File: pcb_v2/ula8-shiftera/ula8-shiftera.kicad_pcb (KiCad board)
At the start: 2 copper layers, 54.4 x 61 mm, 17 parts, among them J1 ula8a, U1 74LS244, U2 74LS244, U3 74LS157, U4 74LS157

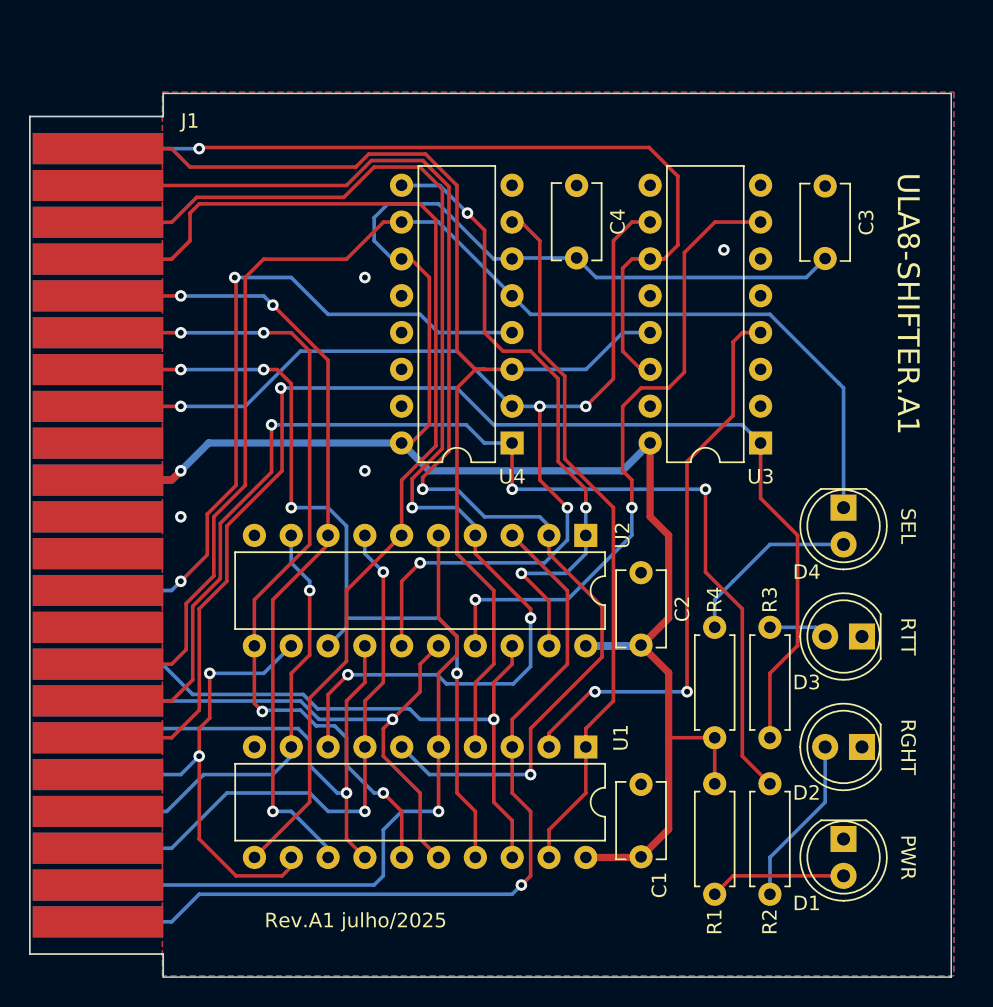
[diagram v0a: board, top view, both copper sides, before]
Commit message: revisao completa; mgrfa agora inclui sr8 e sgrda; remover estes dois no proximo commit
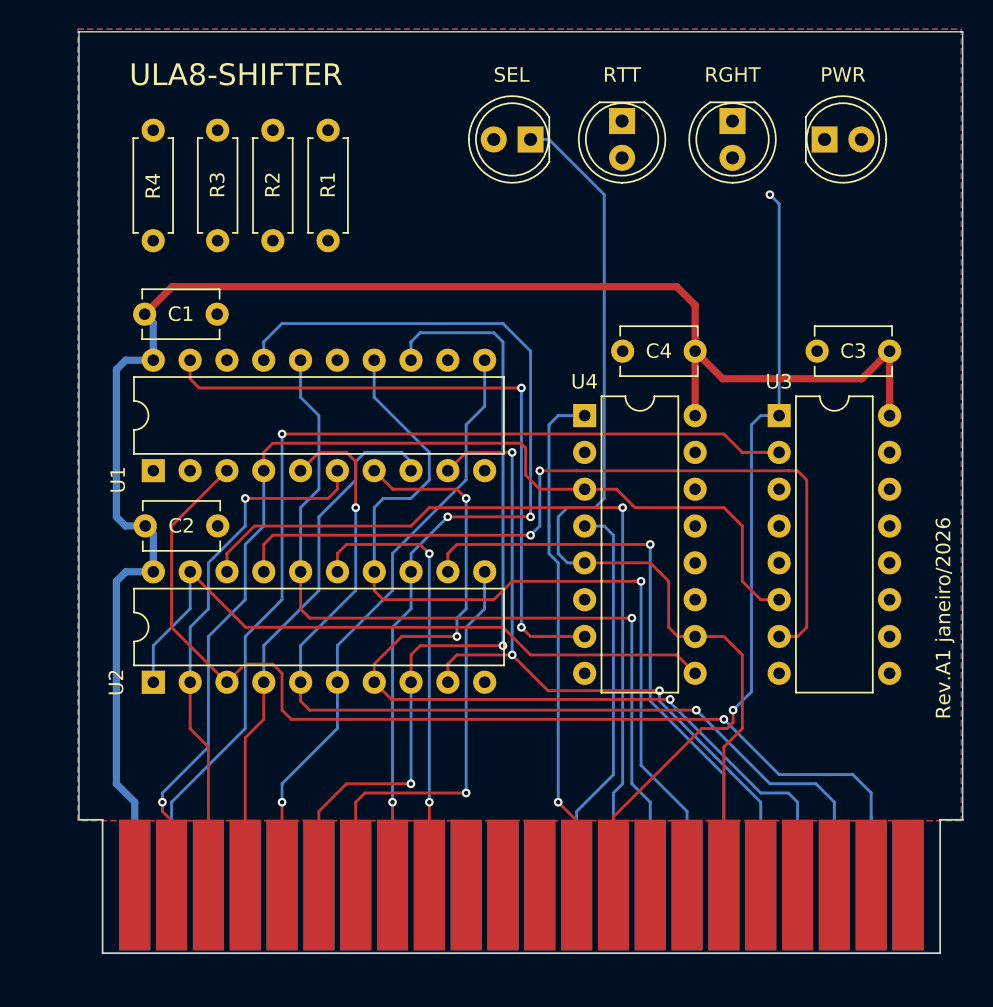
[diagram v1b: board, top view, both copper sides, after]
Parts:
- moved R3 56.6 mm to (41.3, 27.3), turned to -90 degrees
- moved R4 51.7 mm to (36.8, 34.9)
- moved J1 50.9 mm to (35.6, 79.4), turned to 90 degrees
- moved R2 50.8 mm to (45.1, 34.9), turned to 90 degrees
- moved D1 48.3 mm to (83.1, 27.9), turned to 0 degrees
- moved R1 46.0 mm to (48.9, 34.9), turned to 90 degrees
- moved D2 44.1 mm to (76.8, 26.7), turned to -90 degrees
- moved C1 43.7 mm to (41.2, 40.0), turned to 180 degrees
- moved D3 39.2 mm to (69.2, 26.7), turned to -90 degrees
- moved U1 35.4 mm to (36.8, 50.8), turned to 90 degrees
- moved D4 33.3 mm to (62.9, 27.9), turned to 180 degrees
- moved U2 31.5 mm to (36.8, 65.4), turned to 90 degrees
- moved C2 29.4 mm to (41.3, 54.6), turned to 180 degrees
- moved C4 11.9 mm to (69.2, 42.5), turned to 0 degrees
- moved C3 11.4 mm to (82.6, 42.5), turned to 0 degrees
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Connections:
- net n_shift_left renamed ~{shift_left}
- net n_shift_right renamed ~{shift_right}
- D4 pad 1: n_select -> ~{select}
- J1 pad 1: lower_bus0 -> +5V
- J1 pad 10: +5V -> unconnected-(J1-Pin_10-Pad10)
- J1 pad 11: GND -> unconnected-(J1-Pin_11-Pad11)
- J1 pad 13: unconnected-(J1-Pad13) -> option_rigth
- J1 pad 14: unconnected-(J1-Pad14) -> option_rotate
- J1 pad 15: n_select -> unconnected-(J1-Pin_15-Pad15)
- J1 pad 16: option_rigth -> unconnected-(J1-Pin_16-Pad16)
- J1 pad 17: option_rotate -> ~{select}
- J1 pad 2: lower_bus1 -> lower_bus0
- J1 pad 22: unconnected-(J1-Pad22) -> GND
- J1 pad 23: carry_in -> +5V
- J1 pad 24: unconnected-(J1-Pad24) -> carry_in
- J1 pad 3: lower_bus2 -> lower_bus1
- J1 pad 32: +5V -> unconnected-(J1-Pin_32-Pad32)
- J1 pad 33: GND -> unconnected-(J1-Pin_33-Pad33)
- J1 pad 36: unconnected-(J1-Pad36) -> ula_bus0
- J1 pad 37: ula_bus0 -> ula_bus1
- J1 pad 38: ula_bus1 -> ula_bus2
- J1 pad 39: ula_bus2 -> ula_bus3
- J1 pad 4: lower_bus3 -> lower_bus2
- J1 pad 40: ula_bus3 -> ula_bus4
- J1 pad 41: ula_bus4 -> ula_bus5
- J1 pad 42: ula_bus5 -> ula_bus6
- J1 pad 43: ula_bus6 -> ula_bus7
- J1 pad 44: ula_bus7 -> GND
- J1 pad 5: lower_bus4 -> lower_bus3
- J1 pad 6: lower_bus5 -> lower_bus4
- J1 pad 7: lower_bus6 -> lower_bus5
- J1 pad 8: lower_bus7 -> lower_bus6
- J1 pad 9: unconnected-(J1-Pad9) -> lower_bus7
- U3 pad 10: lower_bus7 -> +5V
- U3 pad 11: carry_in -> +5V
- U3 pad 13: lower_bus0 -> +5V
- U3 pad 14: carry_in -> +5V
- U3 pad 2: unconnected-(U3-Pad2) -> carry_in
- U3 pad 3: unconnected-(U3-Pad3) -> lower_bus7
- U3 pad 5: unconnected-(U3-Pad5) -> GND
- U3 pad 6: unconnected-(U3-Pad6) -> lower_bus0
- U4 pad 10: n_select -> ~{select}
- U4 pad 13: unconnected-(U4-Pad13) -> +5V
- U4 pad 14: unconnected-(U4-Pad14) -> +5V
- U4 pad 5: n_select -> ~{select}
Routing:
- net n_select: track 89.7 -> 0.00 mm
- net ~{select}: track 0.00 -> 67.7 mm
- net lower_bus1: track 87.4 -> 36.7 mm, vias 2 -> 1
- net lower_bus7: track 79.2 -> 31.0 mm, vias 5 -> 2
- net option_rigth: track 82.8 -> 35.3 mm, vias 3 -> 1
- net lower_bus2: track 83.9 -> 37.3 mm, vias 3 -> 0
- net Net-(U1-I0a): track 39.3 -> 0.00 mm, vias 2 -> 0
- net +5V: track 149.3 -> 112.7 mm, vias 1 -> 0
- net option_rotate: track 89.3 -> 54.4 mm, vias 1 -> 2
- net lower_bus3: track 75.6 -> 42.0 mm, vias 0 -> 1
- net lower_bus5: track 58.6 -> 29.4 mm, vias 4 -> 1
- net ula_bus2: track 35.9 -> 61.6 mm
- net ula_bus5: track 40.6 -> 63.2 mm, vias 2 -> 3
- net carry_out: track 49.2 -> 27.4 mm, vias 2 -> 0
- net ula_bus1: track 38.6 -> 60.3 mm
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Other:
- board size 54.4 x 61 mm -> 61 x 54.4 mm
- board text added: "Rev.A1 janeiro/2026"
- board text added: "ULA8-SHIFTER"
- board text removed: "Rev.A1 julho/2025"
- board text removed: "ULA8-SHIFTER.A1"

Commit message: entrada de força nas laterais; select agora é posicional, permitindo que a placa seja inserida em qualquer slot
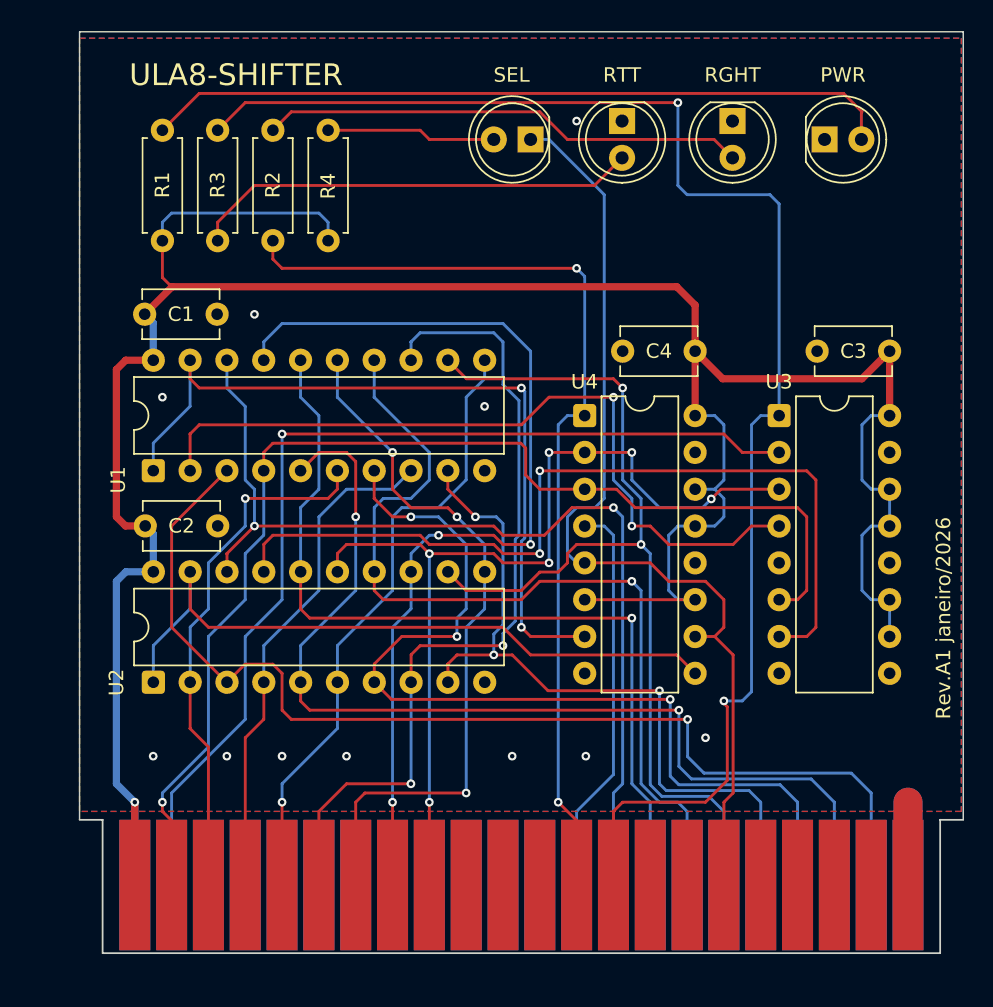
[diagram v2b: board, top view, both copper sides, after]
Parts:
- moved R4 12.1 mm to (48.9, 34.9)
- moved R1 11.4 mm to (37.5, 34.9)
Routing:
- net +5V: track 112.7 -> 186.1 mm, vias 0 -> 1
- net Net-(U1-I0a): track 0.00 -> 53.4 mm, vias 0 -> 2
- net Net-(D1-A): track 0.00 -> 51.8 mm
- net option_rotate: track 54.4 -> 102.8 mm
- net lower_bus7: track 31.0 -> 66.4 mm, vias 2 -> 6
- net Net-(D2-A): track 0.00 -> 33.6 mm
- net option_rigth: track 35.3 -> 67.2 mm, vias 1 -> 2
- net Net-(D3-A): track 0.00 -> 31.0 mm
- net ula_bus3: track 41.1 -> 67.5 mm, vias 1 -> 2
- net lower_bus5: track 29.4 -> 49.7 mm, vias 1 -> 3
- net ula_bus0: track 56.2 -> 68.6 mm, vias 1 -> 2
- net Net-(D4-A): track 0.00 -> 11.7 mm
- net GND: track 0.00 -> 11.4 mm, vias 0 -> 11
- net ~{shift_left}: track 45.5 -> 54.4 mm
- net lower_bus0: track 76.6 -> 81.2 mm
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
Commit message: deslocando alimentação para as estremidades do conector; carry out em três estados (ativo apenas quando select)
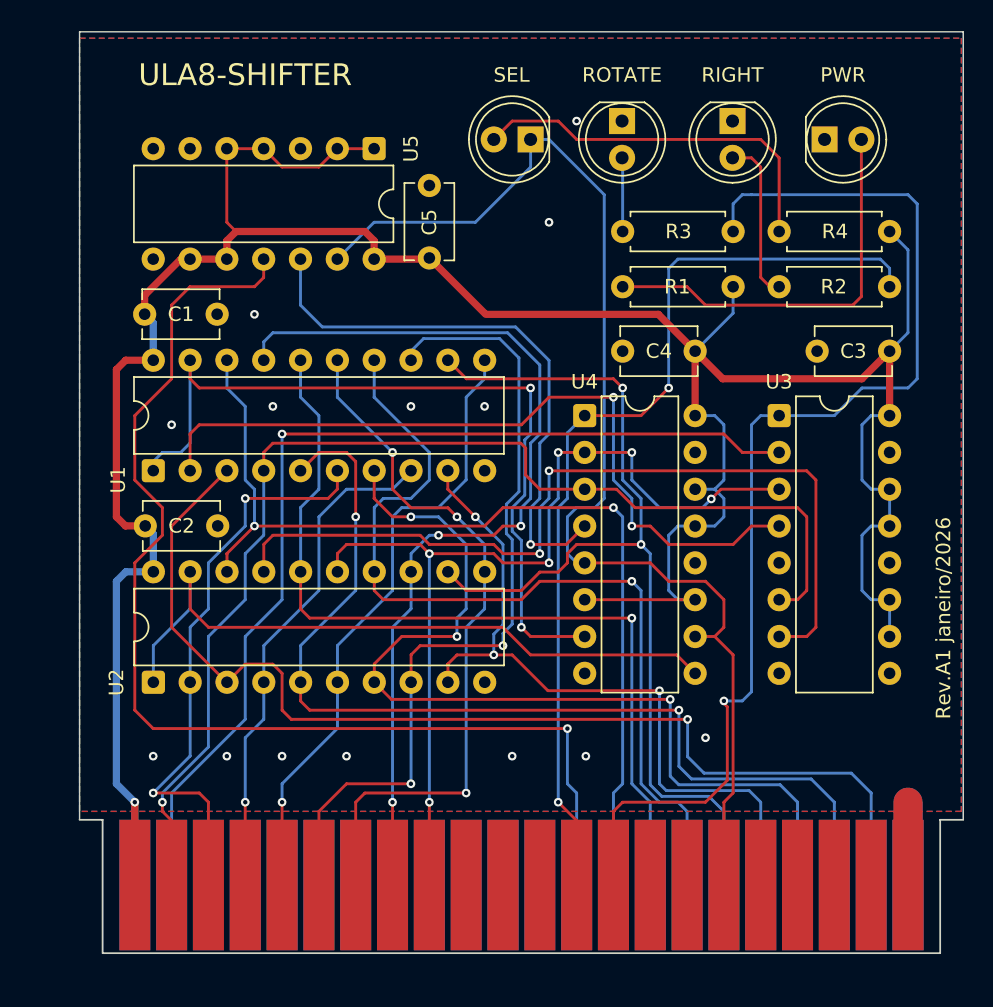
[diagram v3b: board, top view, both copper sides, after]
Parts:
- added C5: 100nF, Capacitor_THT:C_Disc_D5.1mm_W3.2mm_P5.00mm, F.Cu at (55.9, 31.1)
- added U5: 74LS125, Package_DIP:DIP-14_W7.62mm, F.Cu at (52.1, 28.6)
- moved R2 42.7 mm to (87.6, 38.1), turned to 180 degrees
- moved R1 39.5 mm to (76.8, 38.1), turned to 180 degrees
- moved R4 38.7 mm to (87.6, 34.3), turned to 180 degrees
- moved R3 36.2 mm to (76.8, 34.3), turned to 180 degrees
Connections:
- net option_rigth renamed option_right
- U4 pad 4: carry_out -> Net-(U4-Za)
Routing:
- net carry_out: track 27.4 -> 80.4 mm, vias 0 -> 1
- net Net-(U4-Za): track 0.00 -> 39.4 mm, vias 0 -> 1
- net Net-(D3-A): track 31.0 -> 5.10 mm
- net Net-(D1-A): track 51.8 -> 28.1 mm
- net option_rotate: track 102.8 -> 80.2 mm, vias 2 -> 1
- net Net-(D2-A): track 33.6 -> 11.4 mm
- net ~{select}: track 67.4 -> 85.3 mm
- net +5V: track 186.1 -> 203.6 mm
- net Net-(D4-A): track 11.7 -> 26.3 mm
- net lower_bus1: track 36.7 -> 40.6 mm, vias 1 -> 2
- net ~{shift_left}: track 54.4 -> 56.4 mm
- net lower_bus6: track 66.8 -> 64.9 mm
- net option_right: track 67.2 -> 65.5 mm
- net ula_bus4: track 52.2 -> 51.3 mm
- net ula_bus0: track 68.6 -> 68.0 mm
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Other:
- board text added: "RIGHT"
- board text added: "ROTATE"
- board text removed: "RGHT"
- board text removed: "RTT"
